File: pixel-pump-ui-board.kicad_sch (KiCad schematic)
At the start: 36 parts, among them J1 BM10B-SRSS-TB(LF)(SN), SW1 LIFT, SW2 LOW, SW3 REVERSE, SW4 TRIGGER, SW5 DROP, SW6 HIGH, U1 WS2812-2020, U10 WS2812-2020, U11 WS2812-2020, U12 WS2812-2020, U2 WS2812-2020, U3 WS2812-2020, U4 WS2812-2020, U5 WS2812-2020, U6 WS2812-2020, U7 WS2812-2020, U8 WS2812-2020, U9 WS2812-2020

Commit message: Sorted components and updated schematics title
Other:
- title: (none) -> Pixel Pump UI Board
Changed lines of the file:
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@@
 (kicad_sch (version 20211123) (generator eeschema)
   (paper "A4")
+  (title_block
+    (title "Pixel Pump UI Board")
+    (date "2022-01-11")
+    (rev "3")
+  )
   (junction (at 208.28 154.94) (diameter 1.016) (color 0 0 0 0)
   )

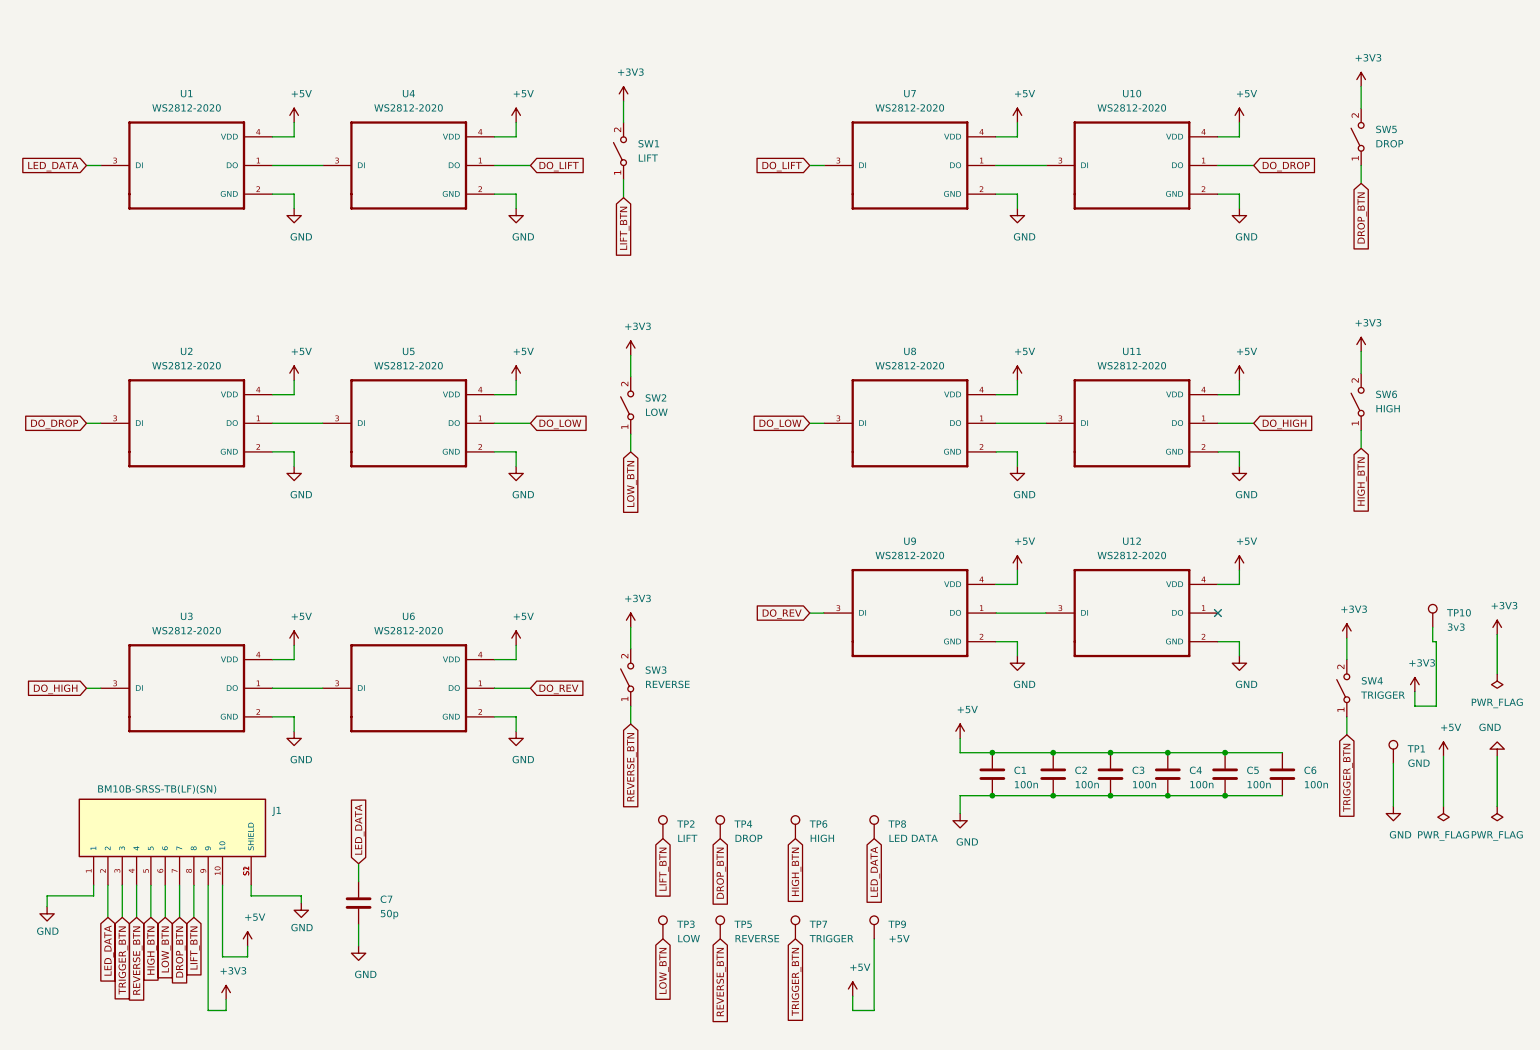
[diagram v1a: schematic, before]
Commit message: Add side load connector to PCB & MPN to all parts
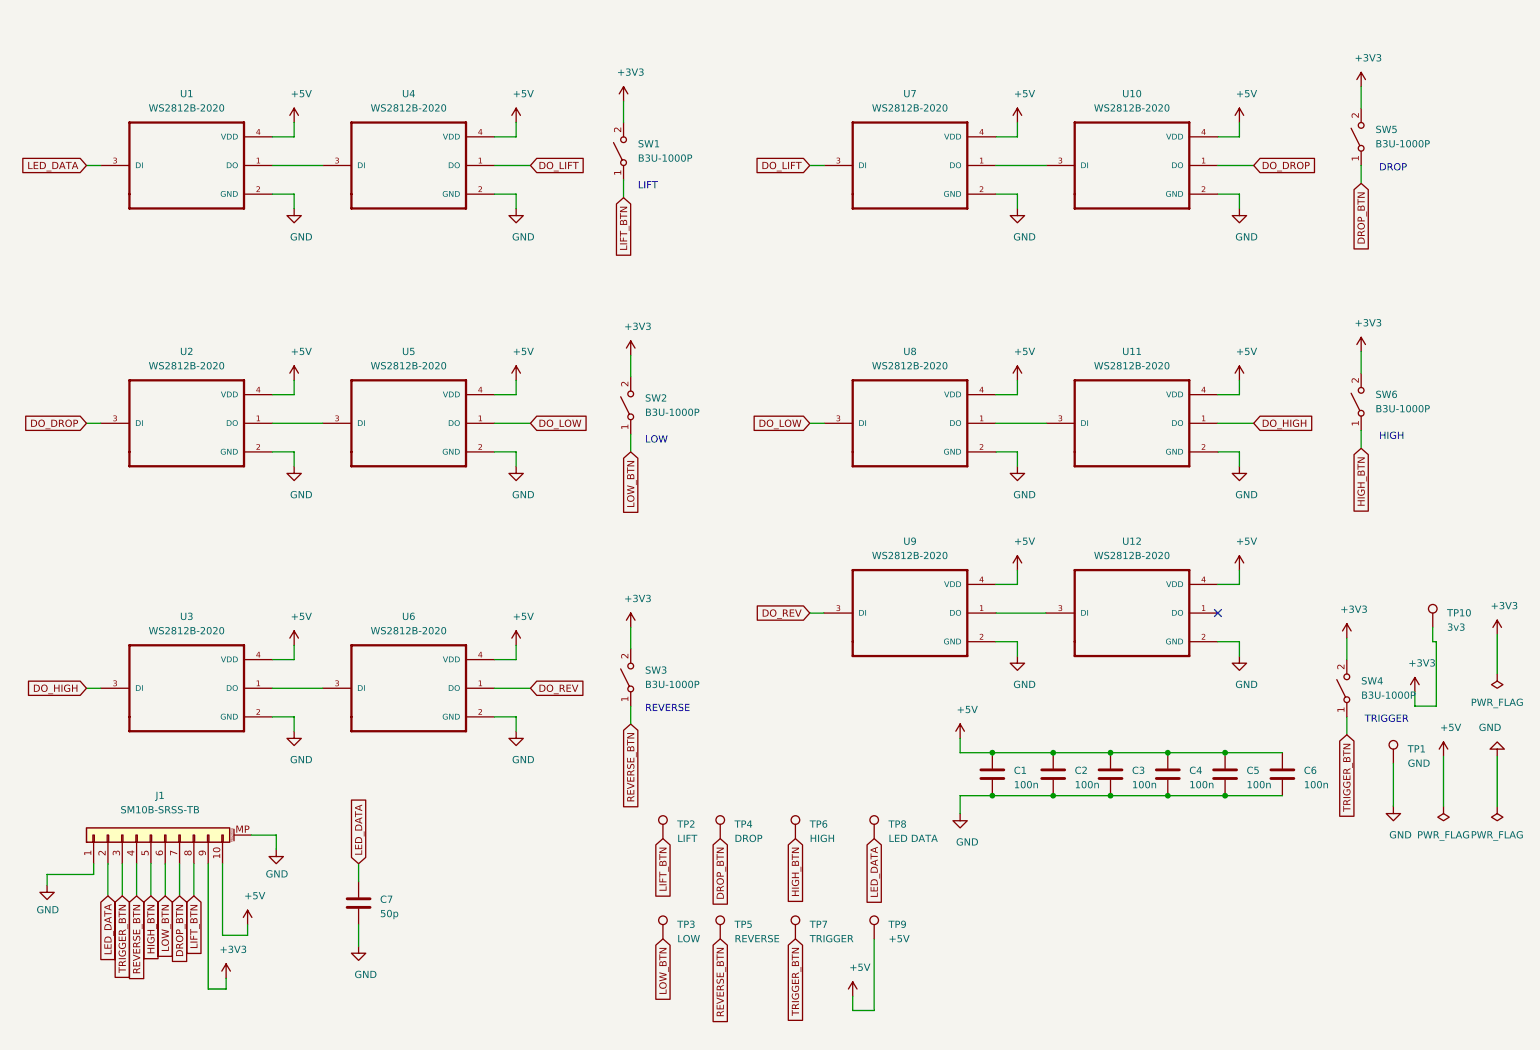
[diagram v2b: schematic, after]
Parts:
- removed J1: BM10B-SRSS-TB(LF)(SN), BM10B-SRSS-TB(LF)(SN):BM10B-SRSS-TB(LF)(SN), symbol BM10B-SRSS-TB(LF)(SN):BM10B-SRSS-TB(LF)(SN)
- added J1: SM10B-SRSS-TB, Connector_JST:JST_SH_SM10B-SRSS-TB_1x10-1MP_P1.00mm_Horizontal, symbol Connector_Generic_MountingPin:Conn_01x10_MountingPin
- C1, C2, C3, C4, C5, C6: MPN (none) -> 100n 0603
- C7: MPN (none) -> 50p 0603
- SW1: value LIFT -> B3U-1000P; MPN (none) -> B3U-1000P
- SW2: value LOW -> B3U-1000P; MPN (none) -> B3U-1000P
- SW3: value REVERSE -> B3U-1000P; MPN (none) -> B3U-1000P
- SW4: value TRIGGER -> B3U-1000P; MPN (none) -> B3U-1000P
- SW5: value DROP -> B3U-1000P; MPN (none) -> B3U-1000P
- SW6: value HIGH -> B3U-1000P; MPN (none) -> B3U-1000P
- U1, U10, U11, U12, U2, U3, U4, U5, U6, U7, U8, U9: value WS2812-2020 -> WS2812B-2020; MPN (none) -> WS2812B-2020
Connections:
- net +3V3: now also J1.9 (Pin_9)
- net +5V: now also J1.10 (Pin_10)
- net DROP_BTN: now also J1.7 (Pin_7)
- net GND: now also J1.1 (Pin_1), J1.MP (MountPin)
- net HIGH_BTN: now also J1.5 (Pin_5)
- net LED_DATA: now also J1.2 (Pin_2)
- net LIFT_BTN: now also J1.8 (Pin_8)
- net LOW_BTN: now also J1.6 (Pin_6)
- net REVERSE_BTN: now also J1.4 (Pin_4)
- net TRIGGER_BTN: now also J1.3 (Pin_3)
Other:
- note added: "DROP"
- note added: "HIGH"
- note added: "LIFT"
- note added: "LOW"
- note added: "REVERSE"
- note added: "TRIGGER"

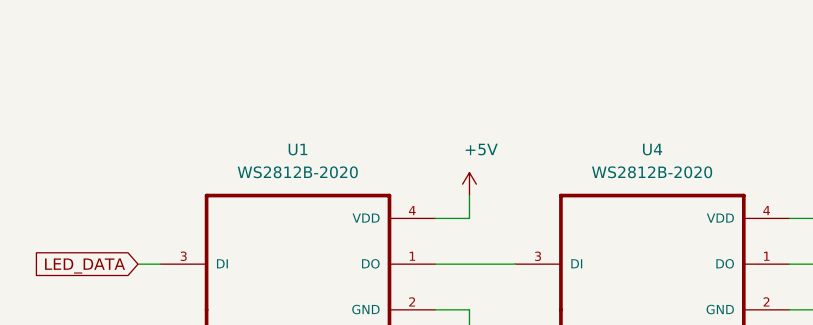
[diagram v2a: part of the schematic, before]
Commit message: Add fiducials and open mounting holes from 2.9 to 3.1 mm
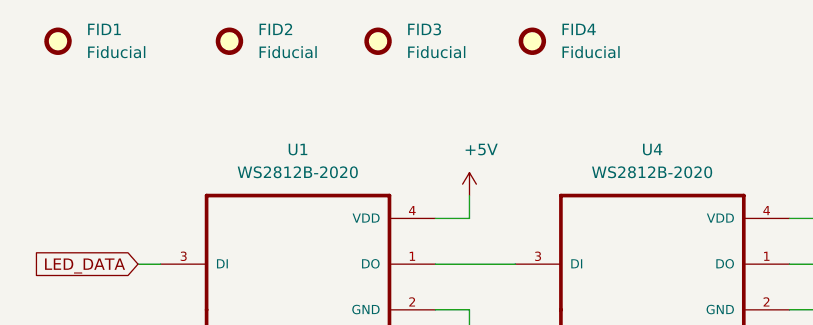
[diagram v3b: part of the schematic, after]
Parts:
- added FID1, FID2, FID3, FID4: Fiducial, Fiducial:Fiducial_0.75mm_Mask1.5mm, symbol Mechanical:Fiducial
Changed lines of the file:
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@@
     (pin "1")
+  )
+  (symbol (lib_id "Mechanical:Fiducial") (at 70.485 18.415 0) (unit 1)
+    (in_bom yes) (on_board yes) (fields_autoplaced)
+    (property "Reference" "FID4" (id 0) (at 73.66 17.1449 0)
+      (effects (font (size 1.27 1.27)) (justify left))
+    )
+    (property "Value" "Fiducial" (id 1) (at 73.66 19.6849 0)
+      (effects (font (size 1.27 1.27)) (justify left))
+    )
+    (property "Footprint" "Fiducial:Fiducial_0.75mm_Mask1.5mm" (id 2) (at 70.485 18.415 0)
+      (effects (font (size 1.27 1.27)) hide)
+    )
+    (property "Datasheet" "~" (id 3) (at 70.485 18.415 0)
+      (effects (font (size 1.27 1.27)) hide)
+    )
   )
   (symbol (lib_id "WS2812-2020:WS2812-2020") (at 212.09 88.9 0) (unit 1)
@@
     (pin "1")
   )
+  (symbol (lib_id "Mechanical:Fiducial") (at 17.78 18.415 0) (unit 1)
+    (in_bom yes) (on_board yes) (fields_autoplaced)
+    (property "Reference" "FID1" (id 0) (at 20.955 17.1449 0)
+      (effects (font (size 1.27 1.27)) (justify left))
+    )
+    (property "Value" "Fiducial" (id 1) (at 20.955 19.6849 0)
+      (effects (font (size 1.27 1.27)) (justify left))
+    )
+    (property "Footprint" "Fiducial:Fiducial_0.75mm_Mask1.5mm" (id 2) (at 17.78 18.415 0)
+      (effects (font (size 1.27 1.27)) hide)
+    )
+    (property "Datasheet" "~" (id 3) (at 17.78 18.415 0)
+      (effects (font (size 1.27 1.27)) hide)
+    )
+  )
   (symbol (lib_id "power:+3V3") (at 252.73 76.2 0) (unit 1)
     (in_bom yes) (on_board yes)
@@
     (pin "1")
   )
+  (symbol (lib_id "Mechanical:Fiducial") (at 36.83 18.415 0) (unit 1)
+    (in_bom yes) (on_board yes) (fields_autoplaced)
+    (property "Reference" "FID2" (id 0) (at 40.005 17.1449 0)
+      (effects (font (size 1.27 1.27)) (justify left))
+    )
+    (property "Value" "Fiducial" (id 1) (at 40.005 19.6849 0)
+      (effects (font (size 1.27 1.27)) (justify left))
+    )
+    (property "Footprint" "Fiducial:Fiducial_0.75mm_Mask1.5mm" (id 2) (at 36.83 18.415 0)
+      (effects (font (size 1.27 1.27)) hide)
+    )
+    (property "Datasheet" "~" (id 3) (at 36.83 18.415 0)
+      (effects (font (size 1.27 1.27)) hide)
+    )
+  )
   (symbol (lib_id "Connector:TestPoint") (at 139.065 180.34 0) (unit 1)
     (in_bom no) (on_board yes)
@@
     (pin "1")
   )
+  (symbol (lib_id "Mechanical:Fiducial") (at 53.34 18.415 0) (unit 1)
+    (in_bom yes) (on_board yes) (fields_autoplaced)
+    (property "Reference" "FID3" (id 0) (at 56.515 17.1449 0)
+      (effects (font (size 1.27 1.27)) (justify left))
+    )
+    (property "Value" "Fiducial" (id 1) (at 56.515 19.6849 0)
+      (effects (font (size 1.27 1.27)) (justify left))
+    )
+    (property "Footprint" "Fiducial:Fiducial_0.75mm_Mask1.5mm" (id 2) (at 53.34 18.415 0)
+      (effects (font (size 1.27 1.27)) hide)
+    )
+    (property "Datasheet" "~" (id 3) (at 53.34 18.415 0)
+      (effects (font (size 1.27 1.27)) hide)
+    )
+  )
   (symbol (lib_id "power:+5V") (at 267.335 147.955 0) (unit 1)
     (in_bom yes) (on_board yes)
@@
       (reference "C7") (unit 1) (value "50p") (footprint "Capacitor_SMD:C_0603_1608Metric")
     )
+    (path "/9af16796-7e03-4894-b0ad-7a8e9338c543"
+      (reference "FID1") (unit 1) (value "Fiducial") (footprint "Fiducial:Fiducial_0.75mm_Mask1.5mm")
+    )
+    (path "/d0d2045d-d03b-4f80-a4bd-74bb5897c12c"
+      (reference "FID2") (unit 1) (value "Fiducial") (footprint "Fiducial:Fiducial_0.75mm_Mask1.5mm")
+    )
+    (path "/ee7c876c-05c3-4cb2-8d5b-b00347eb9f81"
+      (reference "FID3") (unit 1) (value "Fiducial") (footprint "Fiducial:Fiducial_0.75mm_Mask1.5mm")
+    )
+    (path "/0fd172c1-ecd2-43e7-9d61-899bfceaf00c"
+      (reference "FID4") (unit 1) (value "Fiducial") (footprint "Fiducial:Fiducial_0.75mm_Mask1.5mm")
+    )
     (path "/4370c97a-e5e7-4207-a2ef-180e29cc325d"
